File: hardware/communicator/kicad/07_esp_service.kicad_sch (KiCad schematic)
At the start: 3 parts, among them SW1 BOOT

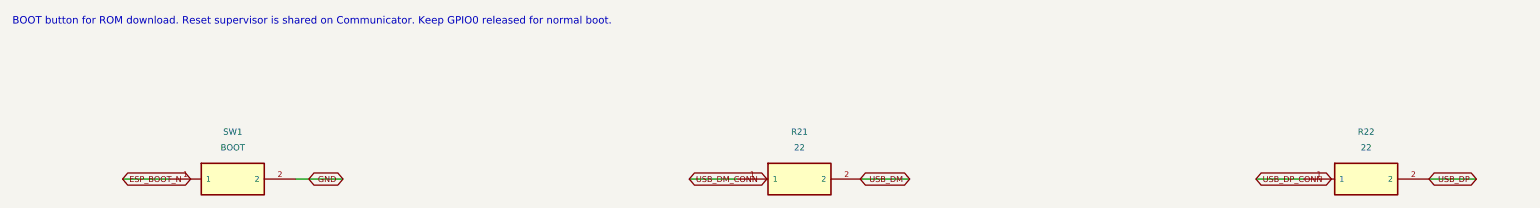
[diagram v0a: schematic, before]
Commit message: feat: add R1 detailed hardware and navigation protocol review candidate
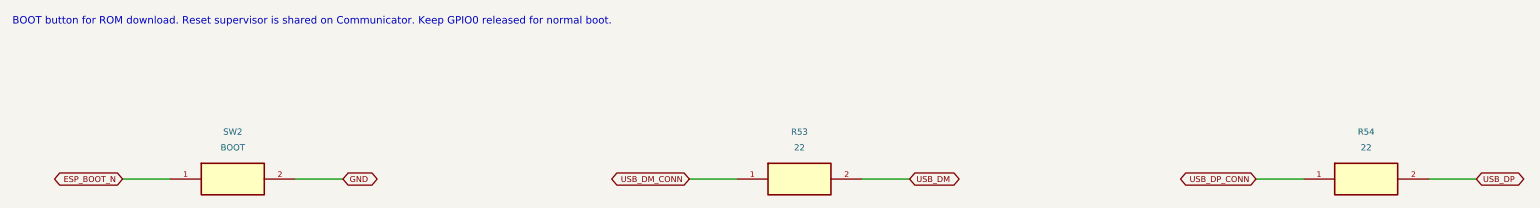
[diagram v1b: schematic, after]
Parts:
- removed R21: 22, CANView:Resistor_SMD__R_0402_1005Metric, symbol CANView:CANView_communicator_R21
- removed R22: 22, CANView:Resistor_SMD__R_0402_1005Metric, symbol CANView:CANView_communicator_R22
- removed SW1: BOOT, CANView:Button_Switch_SMD__SW_SPST_TL3342, symbol CANView:CANView_communicator_SW1
- added R53: 22, CANView:Resistor_SMD__R_0402_1005Metric, symbol CANView:CANView_communicator_R53
- added R54: 22, CANView:Resistor_SMD__R_0402_1005Metric, symbol CANView:CANView_communicator_R54
- added SW2: BOOT, CANView:Button_Switch_SMD__SW_SPST_TL3342, symbol CANView:CANView_communicator_SW2
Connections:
- net ESP_BOOT_N: now also SW2.1
- net GND: now also SW2.2
- net USB_DM: now also R53.2
- net USB_DM_CONN: now also R53.1
- net USB_DP: now also R54.2
- net USB_DP_CONN: now also R54.1
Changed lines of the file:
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@@
 (kicad_sch (version 20250114) (generator "eeschema") (generator_version "10.0") (paper "A3") (title_block (title "CANView / 07_esp_service") (date "2026-09-05") (rev "R1 REVIEW") (company "digitie/canview") (comment 1 "SCHEMATIC REVIEW ONLY - PCB/HIL release gates remain open"))
 (text "BOOT button for ROM download. Reset supervisor is shared on Communicator. Keep GPIO0 released for normal boot." (at 15.24 15.24 0) (effects (font (size 1.2 1.2)) (justify left)))
-(symbol (lib_id "CANView:CANView_communicator_SW1") (at 50.8000 40.6400 0) (unit 1) (in_bom yes) (on_board yes) (dnp no) (property "Reference" "SW1" (at 50.8000 33.0200 0)  (effects (font (size 1.0 1.0)) ))(property "Value" "BOOT" (at 50.8000 35.5600 0)  (effects (font (size 1.0 1.0)) ))(property "Footprint" "CANView:Button_Switch_SMD__SW_SPST_TL3342" (at 50.8000 40.6400 0) (hide yes) (effects (font (size 1.0 1.0)) ))(property "MPN" "TL3342F160QG" (at 50.8000 40.6400 0) (hide yes) (effects (font (size 1.0 1.0)) ))(property "Specification" "Momentary normally open; logic signal only" (at 50.8000 40.6400 0) (hide yes) (effects (font (size 1.0 1.0)) ))(property "Source" "" (at 50.8000 40.6400 0) (hide yes) (effects (font (size 1.0 1.0)) ))(property "Assembly" "FIT" (at 50.8000 40.6400 0) (hide yes) (effects (font (size 1.0 1.0)) ))(instances (project "communicator" (path "/c8ff26d1-0b80-520e-ae3f-45aa29bfe092/5c7d6f70-4127-517d-a353-66a0ef2da52d" (reference "SW1") (unit 1)))))
+(symbol (lib_id "CANView:CANView_communicator_SW2") (at 50.8000 40.6400 0) (unit 1) (in_bom yes) (on_board yes) (dnp no) (property "Reference" "SW2" (at 50.8000 33.0200 0)  (effects (font (size 1.0 1.0)) ))(property "Value" "BOOT" (at 50.8000 35.5600 0)  (effects (font (size 1.0 1.0)) ))(property "Footprint" "CANView:Button_Switch_SMD__SW_SPST_TL3342" (at 50.8000 40.6400 0) (hide yes) (effects (font (size 1.0 1.0)) ))(property "MPN" "TL3342F160QG" (at 50.8000 40.6400 0) (hide yes) (effects (font (size 1.0 1.0)) ))(property "Specification" "Momentary normally open; logic signal only" (at 50.8000 40.6400 0) (hide yes) (effects (font (size 1.0 1.0)) ))(property "Source" "" (at 50.8000 40.6400 0) (hide yes) (effects (font (size 1.0 1.0)) ))(property "Assembly" "FIT" (at 50.8000 40.6400 0) (hide yes) (effects (font (size 1.0 1.0)) ))(instances (project "communicator" (path "/c8ff26d1-0b80-520e-ae3f-45aa29bfe092/5c7d6f70-4127-517d-a353-66a0ef2da52d" (reference "SW2") (unit 1)))))
 (wire (pts (xy 40.6400 40.6400) (xy 33.0200 40.6400)) (stroke (width 0) (type default)))
-(global_label "ESP_BOOT_N" (shape bidirectional) (at 33.0200 40.6400 0) (effects (font (size 0.95 0.95)) (justify left)) (property "Intersheetrefs" "${INTERSHEET_REFS}" (at 33.0200 40.6400 0) (hide yes) (effects (font (size 1.0 1.0)) )))
+(global_label "ESP_BOOT_N" (shape bidirectional) (at 33.0200 40.6400 180) (effects (font (size 0.95 0.95)) (justify right)) (property "Intersheetrefs" "${INTERSHEET_REFS}" (at 33.0200 40.6400 0) (hide yes) (effects (font (size 1.0 1.0)) )))
 (wire (pts (xy 60.9600 40.6400) (xy 68.5800 40.6400)) (stroke (width 0) (type default)))
-(global_label "GND" (shape bidirectional) (at 68.5800 40.6400 180) (effects (font (size 0.95 0.95)) (justify right)) (property "Intersheetrefs" "${INTERSHEET_REFS}" (at 68.5800 40.6400 0) (hide yes) (effects (font (size 1.0 1.0)) )))
-(symbol (lib_id "CANView:CANView_communicator_R21") (at 142.2400 40.6400 0) (unit 1) (in_bom yes) (on_board yes) (dnp no) (property "Reference" "R21" (at 142.2400 33.0200 0)  (effects (font (size 1.0 1.0)) ))(property "Value" "22" (at 142.2400 35.5600 0)  (effects (font (size 1.0 1.0)) ))(property "Footprint" "CANView:Resistor_SMD__R_0402_1005Metric" (at 142.2400 40.6400 0) (hide yes) (effects (font (size 1.0 1.0)) ))(property "MPN" "GEN-R-0402-22-1%" (at 142.2400 40.6400 0) (hide yes) (effects (font (size 1.0 1.0)) ))(property "Specification" "0.1W; 50V; ±1%; ±100ppm/K; -55..155C" (at 142.2400 40.6400 0) (hide yes) (effects (font (size 1.0 1.0)) ))(property "Source" "" (at 142.2400 40.6400 0) (hide yes) (effects (font (size 1.0 1.0)) ))(property "Assembly" "FIT" (at 142.2400 40.6400 0) (hide yes) (effects (font (size 1.0 1.0)) ))(instances (project "communicator" (path "/c8ff26d1-0b80-520e-ae3f-45aa29bfe092/5c7d6f70-4127-517d-a353-66a0ef2da52d" (reference "R21") (unit 1)))))
+(global_label "GND" (shape bidirectional) (at 68.5800 40.6400 0) (effects (font (size 0.95 0.95)) (justify left)) (property "Intersheetrefs" "${INTERSHEET_REFS}" (at 68.5800 40.6400 0) (hide yes) (effects (font (size 1.0 1.0)) )))
+(symbol (lib_id "CANView:CANView_communicator_R53") (at 142.2400 40.6400 0) (unit 1) (in_bom yes) (on_board yes) (dnp no) (property "Reference" "R53" (at 142.2400 33.0200 0)  (effects (font (size 1.0 1.0)) ))(property "Value" "22" (at 142.2400 35.5600 0)  (effects (font (size 1.0 1.0)) ))(property "Footprint" "CANView:Resistor_SMD__R_0402_1005Metric" (at 142.2400 40.6400 0) (hide yes) (effects (font (size 1.0 1.0)) ))(property "MPN" "GEN-R-0402-22-1%" (at 142.2400 40.6400 0) (hide yes) (effects (font (size 1.0 1.0)) ))(property "Specification" "0.1W; 50V; ±1%; ±100ppm/K; -55..155C" (at 142.2400 40.6400 0) (hide yes) (effects (font (size 1.0 1.0)) ))(property "Source" "" (at 142.2400 40.6400 0) (hide yes) (effects (font (size 1.0 1.0)) ))(property "Assembly" "FIT" (at 142.2400 40.6400 0) (hide yes) (effects (font (size 1.0 1.0)) ))(instances (project "communicator" (path "/c8ff26d1-0b80-520e-ae3f-45aa29bfe092/5c7d6f70-4127-517d-a353-66a0ef2da52d" (reference "R53") (unit 1)))))
 (wire (pts (xy 132.0800 40.6400) (xy 124.4600 40.6400)) (stroke (width 0) (type default)))
-(global_label "USB_DM_CONN" (shape bidirectional) (at 124.4600 40.6400 0) (effects (font (size 0.95 0.95)) (justify left)) (property "Intersheetrefs" "${INTERSHEET_REFS}" (at 124.4600 40.6400 0) (hide yes) (effects (font (size 1.0 1.0)) )))
+(global_label "USB_DM_CONN" (shape bidirectional) (at 124.4600 40.6400 180) (effects (font (size 0.95 0.95)) (justify right)) (property "Intersheetrefs" "${INTERSHEET_REFS}" (at 124.4600 40.6400 0) (hide yes) (effects (font (size 1.0 1.0)) )))
 (wire (pts (xy 152.4000 40.6400) (xy 160.0200 40.6400)) (stroke (width 0) (type default)))
-(global_label "USB_DM" (shape bidirectional) (at 160.0200 40.6400 180) (effects (font (size 0.95 0.95)) (justify right)) (property "Intersheetrefs" "${INTERSHEET_REFS}" (at 160.0200 40.6400 0) (hide yes) (effects (font (size 1.0 1.0)) )))
-(symbol (lib_id "CANView:CANView_communicator_R22") (at 233.6800 40.6400 0) (unit 1) (in_bom yes) (on_board yes) (dnp no) (property "Reference" "R22" (at 233.6800 33.0200 0)  (effects (font (size 1.0 1.0)) ))(property "Value" "22" (at 233.6800 35.5600 0)  (effects (font (size 1.0 1.0)) ))(property "Footprint" "CANView:Resistor_SMD__R_0402_1005Metric" (at 233.6800 40.6400 0) (hide yes) (effects (font (size 1.0 1.0)) ))(property "MPN" "GEN-R-0402-22-1%" (at 233.6800 40.6400 0) (hide yes) (effects (font (size 1.0 1.0)) ))(property "Specification" "0.1W; 50V; ±1%; ±100ppm/K; -55..155C" (at 233.6800 40.6400 0) (hide yes) (effects (font (size 1.0 1.0)) ))(property "Source" "" (at 233.6800 40.6400 0) (hide yes) (effects (font (size 1.0 1.0)) ))(property "Assembly" "FIT" (at 233.6800 40.6400 0) (hide yes) (effects (font (size 1.0 1.0)) ))(instances (project "communicator" (path "/c8ff26d1-0b80-520e-ae3f-45aa29bfe092/5c7d6f70-4127-517d-a353-66a0ef2da52d" (reference "R22") (unit 1)))))
+(global_label "USB_DM" (shape bidirectional) (at 160.0200 40.6400 0) (effects (font (size 0.95 0.95)) (justify left)) (property "Intersheetrefs" "${INTERSHEET_REFS}" (at 160.0200 40.6400 0) (hide yes) (effects (font (size 1.0 1.0)) )))
+(symbol (lib_id "CANView:CANView_communicator_R54") (at 233.6800 40.6400 0) (unit 1) (in_bom yes) (on_board yes) (dnp no) (property "Reference" "R54" (at 233.6800 33.0200 0)  (effects (font (size 1.0 1.0)) ))(property "Value" "22" (at 233.6800 35.5600 0)  (effects (font (size 1.0 1.0)) ))(property "Footprint" "CANView:Resistor_SMD__R_0402_1005Metric" (at 233.6800 40.6400 0) (hide yes) (effects (font (size 1.0 1.0)) ))(property "MPN" "GEN-R-0402-22-1%" (at 233.6800 40.6400 0) (hide yes) (effects (font (size 1.0 1.0)) ))(property "Specification" "0.1W; 50V; ±1%; ±100ppm/K; -55..155C" (at 233.6800 40.6400 0) (hide yes) (effects (font (size 1.0 1.0)) ))(property "Source" "" (at 233.6800 40.6400 0) (hide yes) (effects (font (size 1.0 1.0)) ))(property "Assembly" "FIT" (at 233.6800 40.6400 0) (hide yes) (effects (font (size 1.0 1.0)) ))(instances (project "communicator" (path "/c8ff26d1-0b80-520e-ae3f-45aa29bfe092/5c7d6f70-4127-517d-a353-66a0ef2da52d" (reference "R54") (unit 1)))))
 (wire (pts (xy 223.5200 40.6400) (xy 215.9000 40.6400)) (stroke (width 0) (type default)))
-(global_label "USB_DP_CONN" (shape bidirectional) (at 215.9000 40.6400 0) (effects (font (size 0.95 0.95)) (justify left)) (property "Intersheetrefs" "${INTERSHEET_REFS}" (at 215.9000 40.6400 0) (hide yes) (effects (font (size 1.0 1.0)) )))
+(global_label "USB_DP_CONN" (shape bidirectional) (at 215.9000 40.6400 180) (effects (font (size 0.95 0.95)) (justify right)) (property "Intersheetrefs" "${INTERSHEET_REFS}" (at 215.9000 40.6400 0) (hide yes) (effects (font (size 1.0 1.0)) )))
 (wire (pts (xy 243.8400 40.6400) (xy 251.4600 40.6400)) (stroke (width 0) (type default)))
-(global_label "USB_DP" (shape bidirectional) (at 251.4600 40.6400 180) (effects (font (size 0.95 0.95)) (justify right)) (property "Intersheetrefs" "${INTERSHEET_REFS}" (at 251.4600 40.6400 0) (hide yes) (effects (font (size 1.0 1.0)) )))
+(global_label "USB_DP" (shape bidirectional) (at 251.4600 40.6400 0) (effects (font (size 0.95 0.95)) (justify left)) (property "Intersheetrefs" "${INTERSHEET_REFS}" (at 251.4600 40.6400 0) (hide yes) (effects (font (size 1.0 1.0)) )))
 )

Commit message: fix: close hardware rail-fault paths and sensor contract gaps
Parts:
- removed R53: 22, CANView:Resistor_SMD__R_0402_1005Metric, symbol CANView:CANView_communicator_R53
- added R55: 22, CANView:Resistor_SMD__R_0402_1005Metric, symbol CANView:CANView_communicator_R55
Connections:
- net USB_DM: now also R54.2
- net USB_DM_CONN: now also R54.1
- net USB_DP: now also R55.2; no longer R54.2
- net USB_DP_CONN: now also R55.1; no longer R54.1
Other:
- moved on the sheet: R54
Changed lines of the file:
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@@
 (wire (pts (xy 60.9600 40.6400) (xy 68.5800 40.6400)) (stroke (width 0) (type default)))
 (global_label "GND" (shape bidirectional) (at 68.5800 40.6400 0) (effects (font (size 0.95 0.95)) (justify left)) (property "Intersheetrefs" "${INTERSHEET_REFS}" (at 68.5800 40.6400 0) (hide yes) (effects (font (size 1.0 1.0)) )))
-(symbol (lib_id "CANView:CANView_communicator_R53") (at 142.2400 40.6400 0) (unit 1) (in_bom yes) (on_board yes) (dnp no) (property "Reference" "R53" (at 142.2400 33.0200 0)  (effects (font (size 1.0 1.0)) ))(property "Value" "22" (at 142.2400 35.5600 0)  (effects (font (size 1.0 1.0)) ))(property "Footprint" "CANView:Resistor_SMD__R_0402_1005Metric" (at 142.2400 40.6400 0) (hide yes) (effects (font (size 1.0 1.0)) ))(property "MPN" "GEN-R-0402-22-1%" (at 142.2400 40.6400 0) (hide yes) (effects (font (size 1.0 1.0)) ))(property "Specification" "0.1W; 50V; ±1%; ±100ppm/K; -55..155C" (at 142.2400 40.6400 0) (hide yes) (effects (font (size 1.0 1.0)) ))(property "Source" "" (at 142.2400 40.6400 0) (hide yes) (effects (font (size 1.0 1.0)) ))(property "Assembly" "FIT" (at 142.2400 40.6400 0) (hide yes) (effects (font (size 1.0 1.0)) ))(instances (project "communicator" (path "/c8ff26d1-0b80-520e-ae3f-45aa29bfe092/5c7d6f70-4127-517d-a353-66a0ef2da52d" (reference "R53") (unit 1)))))
+(symbol (lib_id "CANView:CANView_communicator_R54") (at 142.2400 40.6400 0) (unit 1) (in_bom yes) (on_board yes) (dnp no) (property "Reference" "R54" (at 142.2400 33.0200 0)  (effects (font (size 1.0 1.0)) ))(property "Value" "22" (at 142.2400 35.5600 0)  (effects (font (size 1.0 1.0)) ))(property "Footprint" "CANView:Resistor_SMD__R_0402_1005Metric" (at 142.2400 40.6400 0) (hide yes) (effects (font (size 1.0 1.0)) ))(property "MPN" "GEN-R-0402-22-1%" (at 142.2400 40.6400 0) (hide yes) (effects (font (size 1.0 1.0)) ))(property "Specification" "0.1W; 50V; ±1%; ±100ppm/K; -55..155C" (at 142.2400 40.6400 0) (hide yes) (effects (font (size 1.0 1.0)) ))(property "Source" "" (at 142.2400 40.6400 0) (hide yes) (effects (font (size 1.0 1.0)) ))(property "Assembly" "FIT" (at 142.2400 40.6400 0) (hide yes) (effects (font (size 1.0 1.0)) ))(instances (project "communicator" (path "/c8ff26d1-0b80-520e-ae3f-45aa29bfe092/5c7d6f70-4127-517d-a353-66a0ef2da52d" (reference "R54") (unit 1)))))
 (wire (pts (xy 132.0800 40.6400) (xy 124.4600 40.6400)) (stroke (width 0) (type default)))
 (global_label "USB_DM_CONN" (shape bidirectional) (at 124.4600 40.6400 180) (effects (font (size 0.95 0.95)) (justify right)) (property "Intersheetrefs" "${INTERSHEET_REFS}" (at 124.4600 40.6400 0) (hide yes) (effects (font (size 1.0 1.0)) )))
 (wire (pts (xy 152.4000 40.6400) (xy 160.0200 40.6400)) (stroke (width 0) (type default)))
 (global_label "USB_DM" (shape bidirectional) (at 160.0200 40.6400 0) (effects (font (size 0.95 0.95)) (justify left)) (property "Intersheetrefs" "${INTERSHEET_REFS}" (at 160.0200 40.6400 0) (hide yes) (effects (font (size 1.0 1.0)) )))
-(symbol (lib_id "CANView:CANView_communicator_R54") (at 233.6800 40.6400 0) (unit 1) (in_bom yes) (on_board yes) (dnp no) (property "Reference" "R54" (at 233.6800 33.0200 0)  (effects (font (size 1.0 1.0)) ))(property "Value" "22" (at 233.6800 35.5600 0)  (effects (font (size 1.0 1.0)) ))(property "Footprint" "CANView:Resistor_SMD__R_0402_1005Metric" (at 233.6800 40.6400 0) (hide yes) (effects (font (size 1.0 1.0)) ))(property "MPN" "GEN-R-0402-22-1%" (at 233.6800 40.6400 0) (hide yes) (effects (font (size 1.0 1.0)) ))(property "Specification" "0.1W; 50V; ±1%; ±100ppm/K; -55..155C" (at 233.6800 40.6400 0) (hide yes) (effects (font (size 1.0 1.0)) ))(property "Source" "" (at 233.6800 40.6400 0) (hide yes) (effects (font (size 1.0 1.0)) ))(property "Assembly" "FIT" (at 233.6800 40.6400 0) (hide yes) (effects (font (size 1.0 1.0)) ))(instances (project "communicator" (path "/c8ff26d1-0b80-520e-ae3f-45aa29bfe092/5c7d6f70-4127-517d-a353-66a0ef2da52d" (reference "R54") (unit 1)))))
+(symbol (lib_id "CANView:CANView_communicator_R55") (at 233.6800 40.6400 0) (unit 1) (in_bom yes) (on_board yes) (dnp no) (property "Reference" "R55" (at 233.6800 33.0200 0)  (effects (font (size 1.0 1.0)) ))(property "Value" "22" (at 233.6800 35.5600 0)  (effects (font (size 1.0 1.0)) ))(property "Footprint" "CANView:Resistor_SMD__R_0402_1005Metric" (at 233.6800 40.6400 0) (hide yes) (effects (font (size 1.0 1.0)) ))(property "MPN" "GEN-R-0402-22-1%" (at 233.6800 40.6400 0) (hide yes) (effects (font (size 1.0 1.0)) ))(property "Specification" "0.1W; 50V; ±1%; ±100ppm/K; -55..155C" (at 233.6800 40.6400 0) (hide yes) (effects (font (size 1.0 1.0)) ))(property "Source" "" (at 233.6800 40.6400 0) (hide yes) (effects (font (size 1.0 1.0)) ))(property "Assembly" "FIT" (at 233.6800 40.6400 0) (hide yes) (effects (font (size 1.0 1.0)) ))(instances (project "communicator" (path "/c8ff26d1-0b80-520e-ae3f-45aa29bfe092/5c7d6f70-4127-517d-a353-66a0ef2da52d" (reference "R55") (unit 1)))))
 (wire (pts (xy 223.5200 40.6400) (xy 215.9000 40.6400)) (stroke (width 0) (type default)))
 (global_label "USB_DP_CONN" (shape bidirectional) (at 215.9000 40.6400 180) (effects (font (size 0.95 0.95)) (justify right)) (property "Intersheetrefs" "${INTERSHEET_REFS}" (at 215.9000 40.6400 0) (hide yes) (effects (font (size 1.0 1.0)) )))

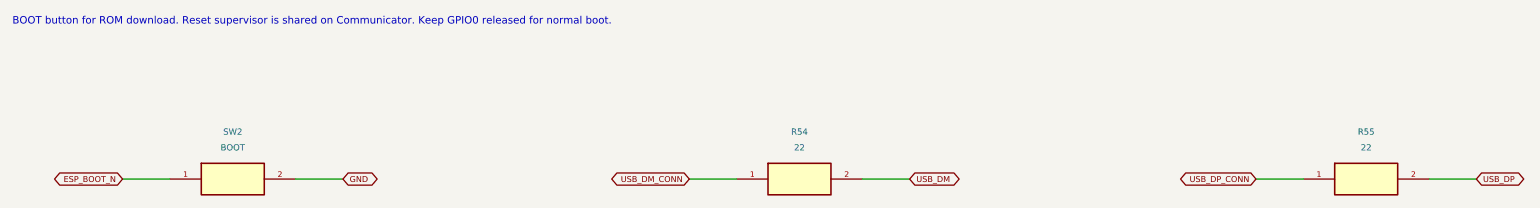
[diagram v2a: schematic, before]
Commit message: Design independent OTA recovery and update N16R8 hardware
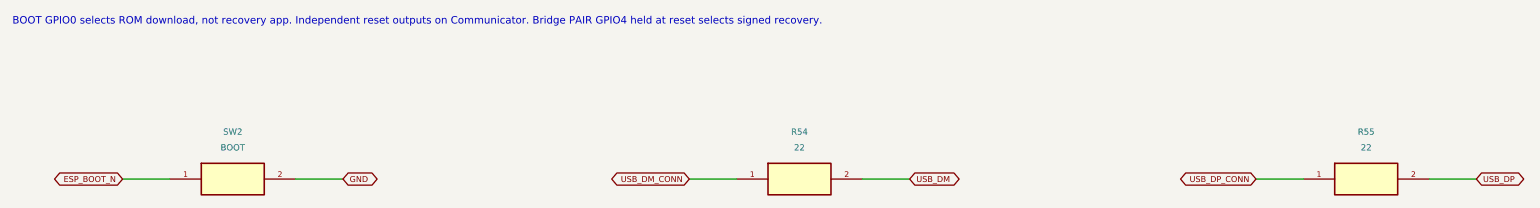
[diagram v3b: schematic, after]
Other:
- note added: "BOOT GPIO0 selects ROM download, not recovery app. Independent reset outputs on Communicator. Bridge PAIR GPIO4 held at reset selects signed recovery."
- note removed: "BOOT button for ROM download. Reset supervisor is shared on Communicator. Keep GPIO0 released for normal boot."
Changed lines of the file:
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@@
 (kicad_sch (version 20250114) (generator "eeschema") (generator_version "10.0") (paper "A3") (title_block (title "CANView / 07_esp_service") (date "2026-09-05") (rev "R1 REVIEW") (company "digitie/canview") (comment 1 "SCHEMATIC REVIEW ONLY - PCB/HIL release gates remain open"))
-(text "BOOT button for ROM download. Reset supervisor is shared on Communicator. Keep GPIO0 released for normal boot." (at 15.24 15.24 0) (effects (font (size 1.2 1.2)) (justify left)))
+(text "BOOT GPIO0 selects ROM download, not recovery app. Independent reset outputs on Communicator. Bridge PAIR GPIO4 held at reset selects signed recovery." (at 15.24 15.24 0) (effects (font (size 1.2 1.2)) (justify left)))
 (symbol (lib_id "CANView:CANView_communicator_SW2") (at 50.8000 40.6400 0) (unit 1) (in_bom yes) (on_board yes) (dnp no) (property "Reference" "SW2" (at 50.8000 33.0200 0)  (effects (font (size 1.0 1.0)) ))(property "Value" "BOOT" (at 50.8000 35.5600 0)  (effects (font (size 1.0 1.0)) ))(property "Footprint" "CANView:Button_Switch_SMD__SW_SPST_TL3342" (at 50.8000 40.6400 0) (hide yes) (effects (font (size 1.0 1.0)) ))(property "MPN" "TL3342F160QG" (at 50.8000 40.6400 0) (hide yes) (effects (font (size 1.0 1.0)) ))(property "Specification" "Momentary normally open; logic signal only" (at 50.8000 40.6400 0) (hide yes) (effects (font (size 1.0 1.0)) ))(property "Source" "" (at 50.8000 40.6400 0) (hide yes) (effects (font (size 1.0 1.0)) ))(property "Assembly" "FIT" (at 50.8000 40.6400 0) (hide yes) (effects (font (size 1.0 1.0)) ))(instances (project "communicator" (path "/c8ff26d1-0b80-520e-ae3f-45aa29bfe092/5c7d6f70-4127-517d-a353-66a0ef2da52d" (reference "SW2") (unit 1)))))
 (wire (pts (xy 40.6400 40.6400) (xy 33.0200 40.6400)) (stroke (width 0) (type default)))
